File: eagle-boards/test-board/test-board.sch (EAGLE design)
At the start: 17 parts

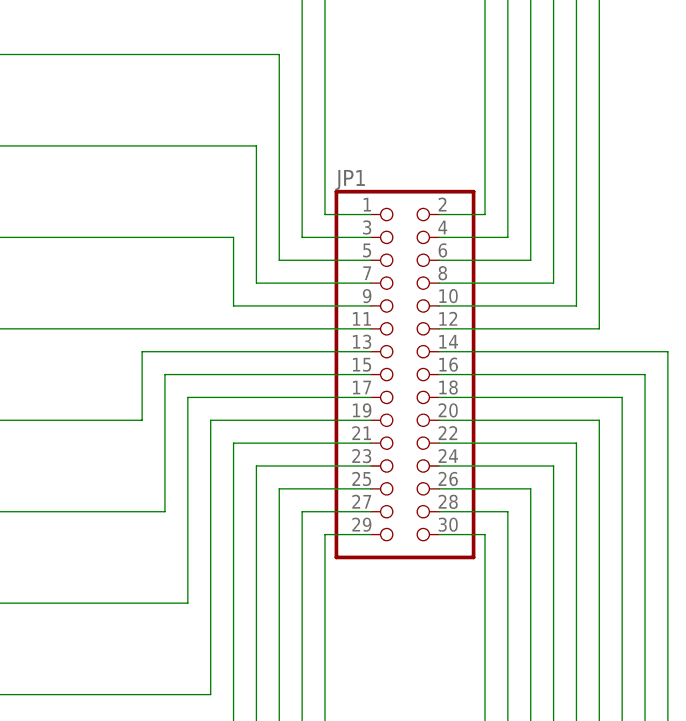
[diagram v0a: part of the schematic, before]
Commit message: Update the test board.
The new revision is smaller, and reports the connector on the bottom side as expected.
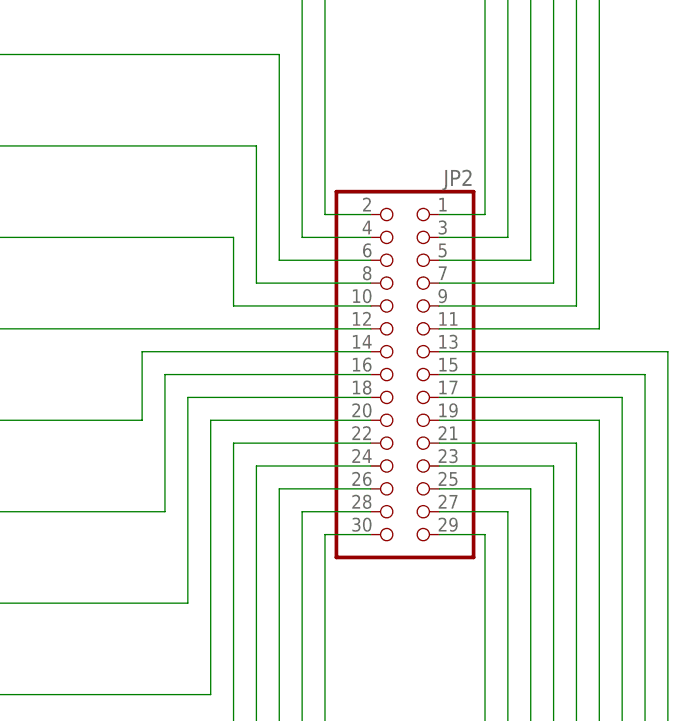
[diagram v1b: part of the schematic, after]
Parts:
- removed JP1: (no value), pinhead:PINHD-2X15
- added JP2: (no value), pinhead:PINHD-2X15
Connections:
- net N$1: now also JP2.2; no longer JP1.1
- net N$10: now also JP2.24; no longer JP1.23
- net N$11: now also JP2.22; no longer JP1.21
- net N$12: now also JP2.20; no longer JP1.19
- net N$13: now also JP2.18; no longer JP1.17
- net N$14: now also JP2.16; no longer JP1.15
- net N$15: now also JP2.14; no longer JP1.13
- net N$16: now also JP2.1; no longer JP1.2
- net N$17: now also JP2.3; no longer JP1.4
- net N$18: now also JP2.5; no longer JP1.6
- net N$19: now also JP2.7; no longer JP1.8
- net N$2: now also JP2.4; no longer JP1.3
- net N$20: now also JP2.9; no longer JP1.10
- net N$21: now also JP2.11; no longer JP1.12
- net N$22: now also JP2.29; no longer JP1.30
- net N$23: now also JP2.27; no longer JP1.28
- net N$24: now also JP2.25; no longer JP1.26
- net N$25: now also JP2.23; no longer JP1.24
- net N$26: now also JP2.21; no longer JP1.22
- net N$27: now also JP2.19; no longer JP1.20
- net N$28: now also JP2.17; no longer JP1.18
- net N$29: now also JP2.15; no longer JP1.16
- net N$3: now also JP2.6; no longer JP1.5
- net N$30: now also JP2.13; no longer JP1.14
- net N$4: now also JP2.8; no longer JP1.7
- net N$5: now also JP2.10; no longer JP1.9
- net N$6: now also JP2.12; no longer JP1.11
- net N$7: now also JP2.30; no longer JP1.29
- net N$8: now also JP2.28; no longer JP1.27
- net N$9: now also JP2.26; no longer JP1.25
